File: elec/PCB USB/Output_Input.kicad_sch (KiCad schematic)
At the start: 8 parts, among them J2 Conn_I2C_Écran, SW3 RotaryEncoder_Switch

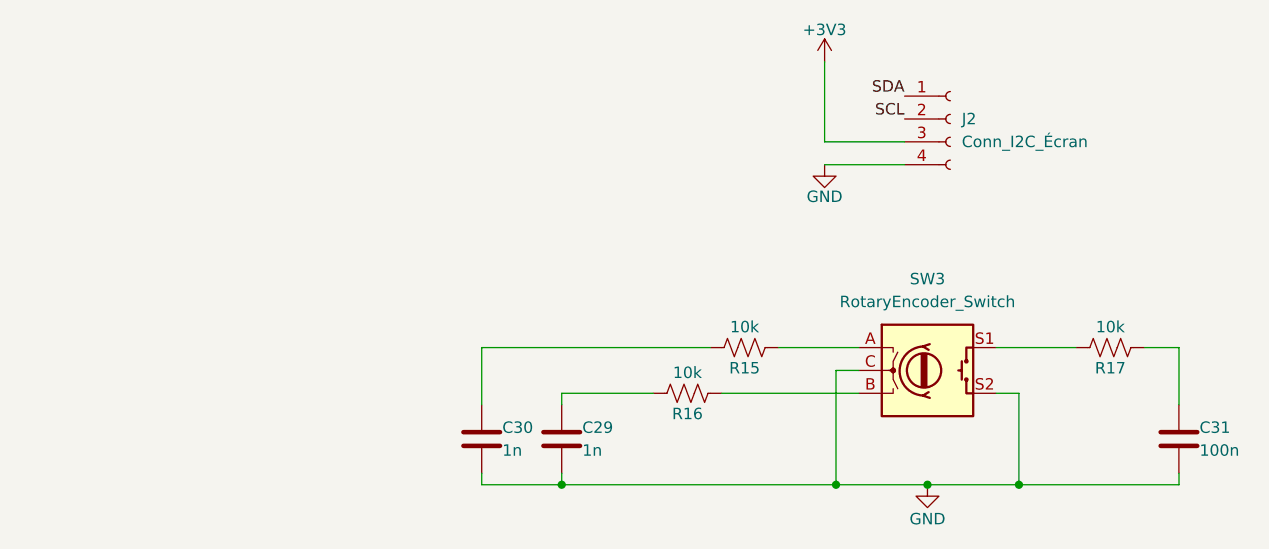
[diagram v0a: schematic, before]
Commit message: push sélection pièces et schéma électrique clean up
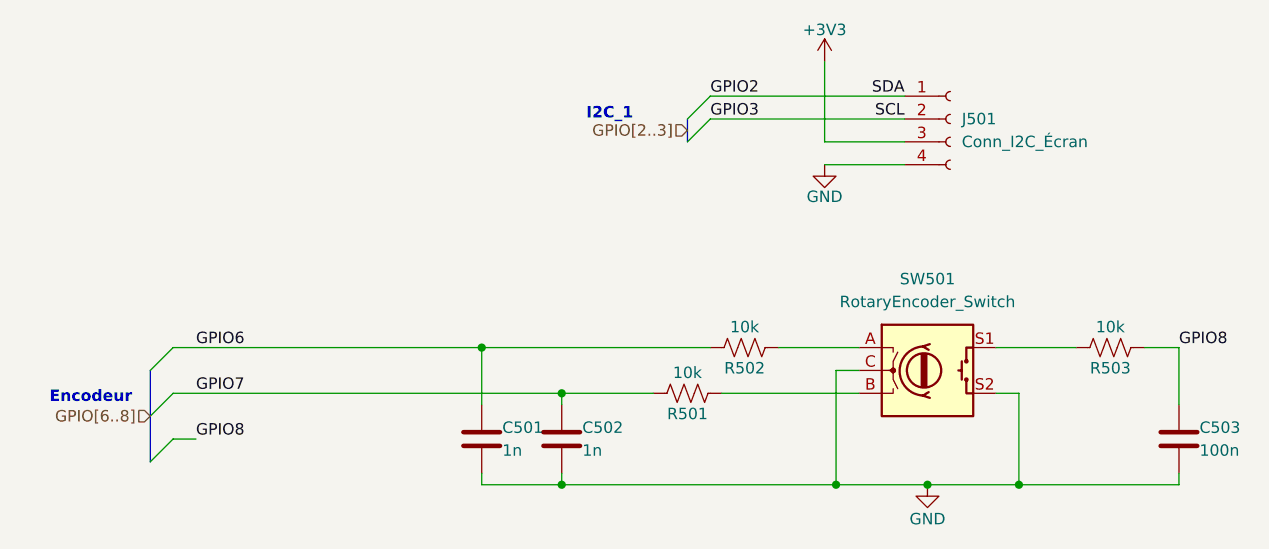
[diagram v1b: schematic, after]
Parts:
- C501: renamed from C30; footprint (none) -> Capacitor_SMD:C_0603_1608Metric
- C502: renamed from C29; footprint (none) -> Capacitor_SMD:C_0603_1608Metric
- C503: renamed from C31; footprint (none) -> Capacitor_SMD:C_0603_1608Metric
- R501: renamed from R16; footprint (none) -> Resistor_SMD:R_0603_1608Metric
- R502: renamed from R15; footprint (none) -> Resistor_SMD:R_0603_1608Metric
- R503: renamed from R17; footprint (none) -> Resistor_SMD:R_0603_1608Metric
- SW501: renamed from SW3; footprint (none) -> Rotary_Encoder:RotaryEncoder_Bourns_Horizontal_PEC12R-2x17F-Sxxxx
- renumbered J2 to J501
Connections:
- net GPIO6: now reaches C501.1, R502.1
- net GPIO7: now reaches C502.1, R501.1
- net GPIO8: now reaches C503.1, R503.2
- net SCL renamed GPIO3
- net SDA renamed GPIO2
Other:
- note added: "Encodeur"
- note added: "I2C_1"

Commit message: Push non terminé
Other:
- company: (none) -> C3I
- title: (none) -> Hub USB2.0 Pomodoro
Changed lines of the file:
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@@
 	(generator_version "9.0")
 	(paper "A4")
+	(title_block
+		(title "Hub USB2.0 Pomodoro")
+		(date "2025-04-20")
+		(rev "1.0")
+		(company "C3I")
+		(comment 1 "Jacob Turcotte")
+		(comment 2 "&")
+		(comment 3 "Charles-Ariel Dion")
+		(comment 4 "Par: Équipe 3")
+	)
 	(text "I2C_1\n"
 		(exclude_from_sim no)

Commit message: push???
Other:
- note added: "GPIO12"
- note added: "GPIO13"
- note added: "GPIO14"
- note added: "X"
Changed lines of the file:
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@@
+		)
+	)
+	(text "X"
+		(exclude_from_sim no)
+		(at 94.488 84.328 0)
+		(effects
+			(font
+				(size 1.27 1.27)
+				(thickness 0.254)
+				(bold yes)
+				(color 255 24 7 1)
+			)
+		)
+	)
+	(text "GPIO13"
+		(exclude_from_sim no)
+		(at 94.234 71.882 0)
+		(effects
+			(font
+				(size 1.27 1.27)
+				(thickness 0.254)
+				(bold yes)
+				(color 34 86 25 1)
+			)
+		)
+	)
+	(text "X"
+		(exclude_from_sim no)
+		(at 94.488 74.168 0)
+		(effects
+			(font
+				(size 1.27 1.27)
+				(thickness 0.254)
+				(bold yes)
+				(color 255 24 7 1)
+			)
+		)
+	)
+	(text "GPIO14"
+		(exclude_from_sim no)
+		(at 94.488 82.55 0)
+		(effects
+			(font
+				(size 1.27 1.27)
+				(thickness 0.254)
+				(bold yes)
+				(color 34 86 25 1)
+			)
+		)
+	)
+	(text "GPIO12"
+		(exclude_from_sim no)
+		(at 94.234 76.962 0)
+		(effects
+			(font
+				(size 1.27 1.27)
+				(thickness 0.254)
+				(bold yes)
+				(color 34 86 25 1)
+			)
 		)
 	)
@@
 			)
 		)
+	)
+	(text "X"
+		(exclude_from_sim no)
+		(at 94.234 78.994 0)
+		(effects
+			(font
+				(size 1.27 1.27)
+				(thickness 0.254)
+				(bold yes)
+				(color 255 24 7 1)
+			)
+		)
